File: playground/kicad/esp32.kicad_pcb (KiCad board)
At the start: 2 copper layers, 85 x 75 mm, 79 parts, among them J1 5 / 12V, J10 Red, J11 Green, J12 Blue, J13 White, J14 Pad, J15 CONN FT232RL, J16 RJ12-I2C, J17 RJ12-I2C, J18 BATT, J2 +12V, J3 Onewire, J4 Onewire, J5 hole, J6 hole, J7 hole, J8 hole, J9 IO_RGBW, Q1 BSP75, Q2 BSP75, Q3 BSP75, Q4 BSP75, SW1 RESET, SW2 PROG, U1 ESP32-WROOM-32U, U2 MS5637, U3 Si7020-A20, U4 MCP73831-2, U5 ACT4088, U6 ACT4088, U7 DS18B20U, U8 TCS3400

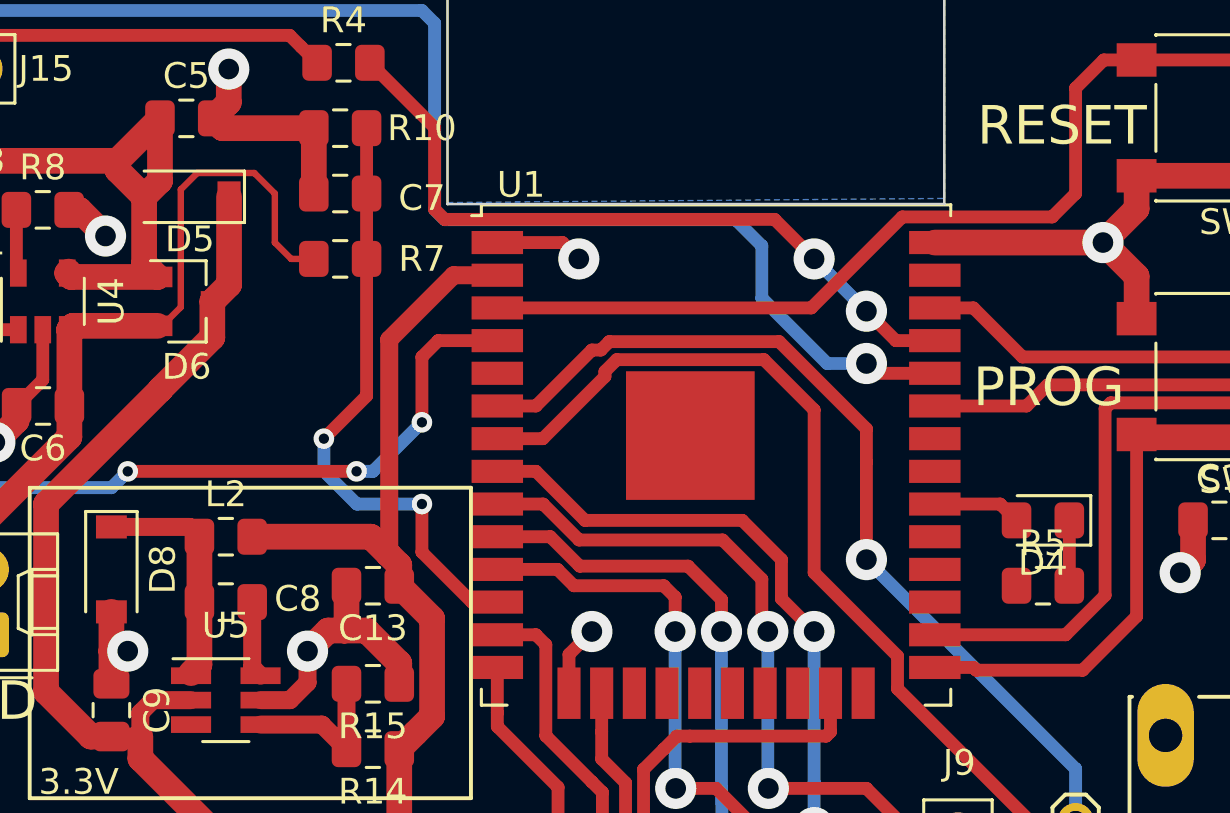
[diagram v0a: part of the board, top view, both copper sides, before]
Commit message: fix missing ground
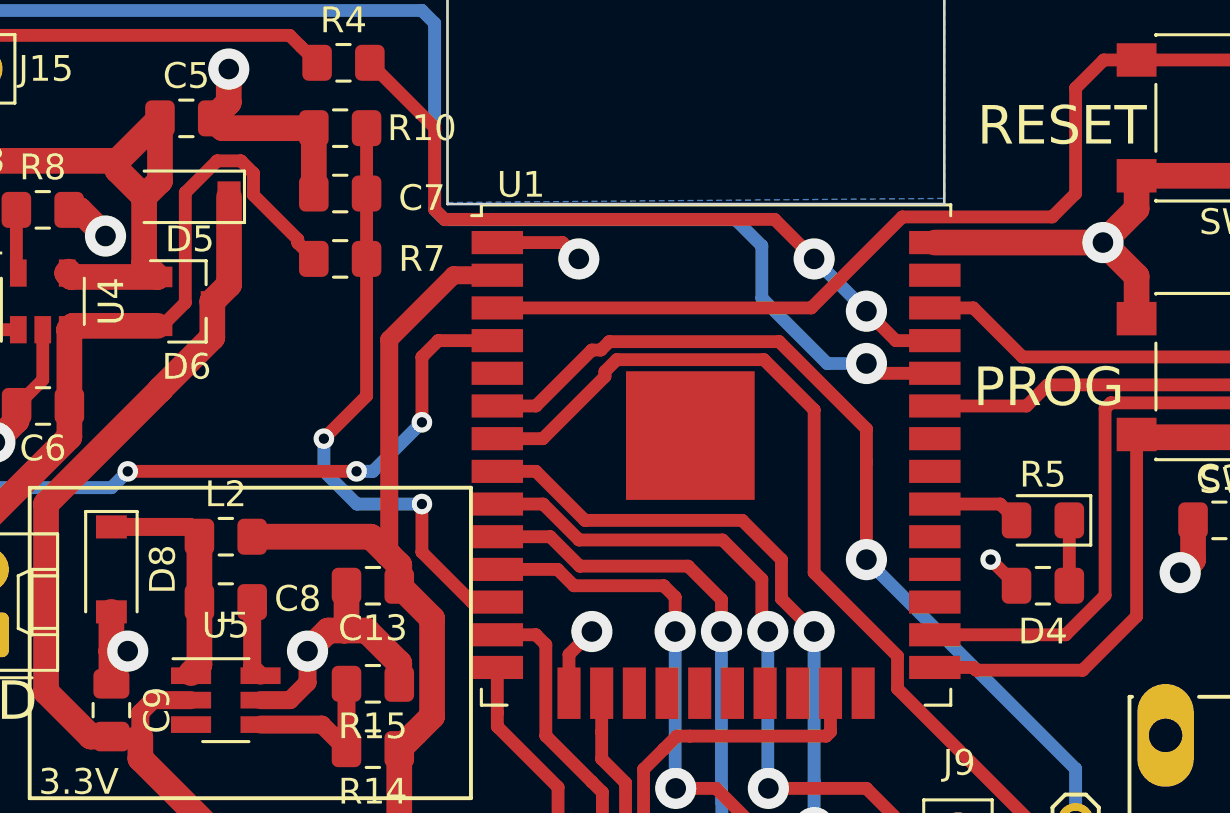
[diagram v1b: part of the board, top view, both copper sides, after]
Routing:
- net GND: track 113.9 -> 115.4 mm, vias 24 -> 25
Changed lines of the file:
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@@
     (thickness 1.6)
     (drawings 52)
-    (tracks 669)
+    (tracks 673)
     (zones 0)
     (modules 79)
@@
   )
   (setup
-    (last_trace_width 0.25)
+    (last_trace_width 0.5)
     (user_trace_width 0.25)
     (user_trace_width 0.5)
@@
     (tags "resistor handsolder")
     (attr smd)
-    (fp_text reference R5 (at 0 -1.65) (layer F.SilkS)
+    (fp_text reference R5 (at 0 -4.318) (layer F.SilkS)
       (effects (font (size 1 1) (thickness 0.15)))
     )
@@
     (tags "LED handsolder")
     (attr smd)
-    (fp_text reference D4 (at 0 -1.65 180) (layer F.SilkS)
+    (fp_text reference D4 (at 0 -4.318 180) (layer F.SilkS)
       (effects (font (size 1 1) (thickness 0.15)))
     )
@@
   (segment (start 158 120.881) (end 158.01 120.871) (width 0.25) (layer F.Cu) (net 1))
   (segment (start 158 122.075) (end 158 120.881) (width 0.25) (layer F.Cu) (net 1))
+  (segment (start 140.475 84.921) (end 139.468 83.914) (width 0.5) (layer F.Cu) (net 1))
+  (via (at 139.468 83.914) (size 0.8) (drill 0.4) (layers F.Cu B.Cu) (net 1))
+  (segment (start 140.475 84.93) (end 140.475 84.921) (width 0.5) (layer F.Cu) (net 1))
   (segment (start 103.738 72.931) (end 103.588 72.781) (width 1) (layer F.Cu) (net 2))
   (segment (start 107.1 72.931) (end 103.738 72.931) (width 1) (layer F.Cu) (net 2))
@@
   (segment (start 132.864 109.822) (end 138.198 109.822) (width 1.5) (layer F.Cu) (net 19))
   (segment (start 127.657 104.615) (end 132.864 109.822) (width 1.5) (layer F.Cu) (net 19))
-  (segment (start 107.276 74.831) (end 107.226 74.831) (width 0.25) (layer F.Cu) (net 19))
-  (segment (start 108.001001 74.105999) (end 107.276 74.831) (width 0.25) (layer F.Cu) (net 19))
-  (segment (start 108.001001 69.533999) (end 108.001001 74.105999) (width 0.25) (layer F.Cu) (net 19))
-  (segment (start 108.643001 68.891999) (end 108.001001 69.533999) (width 0.25) (layer F.Cu) (net 19))
-  (segment (start 110.856999 68.891999) (end 108.643001 68.891999) (width 0.25) (layer F.Cu) (net 19))
-  (segment (start 111.655 69.69) (end 110.856999 68.891999) (width 0.25) (layer F.Cu) (net 19))
-  (segment (start 111.655 71.595) (end 111.655 69.69) (width 0.25) (layer F.Cu) (net 19))
-  (segment (start 112.29 72.23) (end 111.655 71.595) (width 0.25) (layer F.Cu) (net 19))
-  (segment (start 113.17 72.23) (end 112.29 72.23) (width 0.25) (layer F.Cu) (net 19))
   (segment (start 100.225 82.59793) (end 100.225 84.295) (width 1) (layer F.Cu) (net 19))
   (segment (start 103.672 79.15093) (end 100.225 82.59793) (width 1) (layer F.Cu) (net 19))
@@
   (segment (start 97.05 91.28) (end 97.685 91.28) (width 1.5) (layer F.Cu) (net 19))
   (segment (start 95.984802 91.28) (end 97.05 91.28) (width 1.5) (layer F.Cu) (net 19))
+  (segment (start 112.546628 71.606628) (end 112.546628 71.470628) (width 0.5) (layer F.Cu) (net 19))
+  (segment (start 113.17 72.23) (end 112.546628 71.606628) (width 0.5) (layer F.Cu) (net 19))
+  (segment (start 110.82601 68.907008) (end 110.339002 68.42) (width 0.5) (layer F.Cu) (net 19))
+  (segment (start 110.82601 69.75001) (end 110.82601 68.907008) (width 0.5) (layer F.Cu) (net 19))
+  (segment (start 112.546628 71.470628) (end 110.82601 69.75001) (width 0.5) (layer F.Cu) (net 19))
+  (segment (start 107.276 74.831) (end 107.226 74.831) (width 0.5) (layer F.Cu) (net 19))
+  (segment (start 108.176 73.931) (end 107.276 74.831) (width 0.5) (layer F.Cu) (net 19))
+  (segment (start 108.176 69.656998) (end 108.176 73.931) (width 0.5) (layer F.Cu) (net 19))
+  (segment (start 109.412998 68.42) (end 108.176 69.656998) (width 0.5) (layer F.Cu) (net 19))
+  (segment (start 110.339002 68.42) (end 109.412998 68.42) (width 0.5) (layer F.Cu) (net 19))
   (segment (start 121.8 77.945) (end 123.974 75.771) (width 0.5) (layer F.Cu) (net 21))
   (segment (start 120.3 77.945) (end 121.8 77.945) (width 0.5) (layer F.Cu) (net 21))

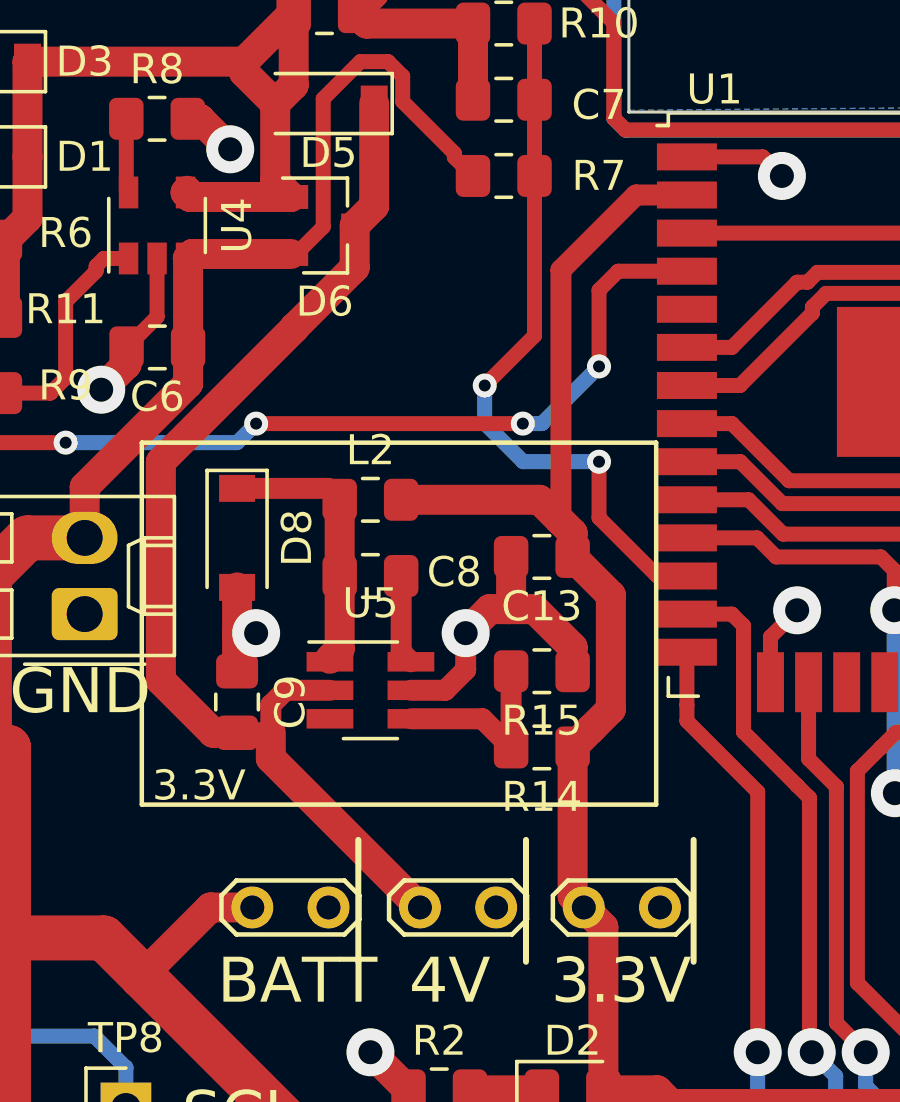
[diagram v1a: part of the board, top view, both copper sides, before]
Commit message: fix: close https://github.com/Hackuarium/esp-32wroom/issues/13
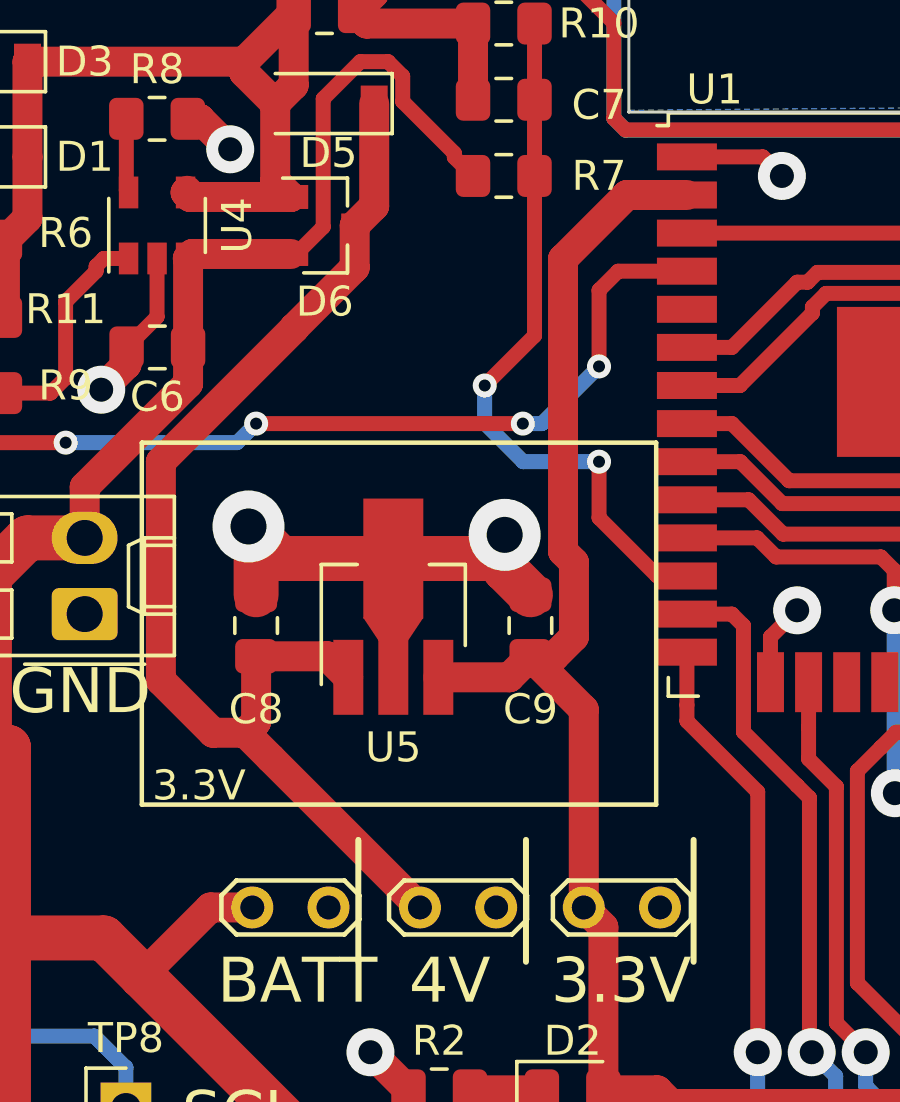
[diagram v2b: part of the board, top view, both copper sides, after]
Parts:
- removed C13: 22µF, Capacitor_SMD:C_0805_2012Metric_Pad1.15x1.40mm_HandSolder
- removed D8: B240A, Diode_SMD:D_SOD-123
- removed L2: 4.7µH, Inductor_SMD:L_0805_2012Metric_Pad1.15x1.40mm_HandSolder
- removed R14: 49.9k, Resistor_SMD:R_0805_2012Metric_Pad1.15x1.40mm_HandSolder
- removed R15: 16.23k, Resistor_SMD:R_0805_2012Metric_Pad1.15x1.40mm_HandSolder
- C8: value 22nF -> C
- C9: value 10µF -> C
- R4: value 499 -> 1k
- U5: value ACT4088 -> AP7365-33YG; footprint Package_TO_SOT_SMD:SOT-23-6_Handsoldering -> Package_TO_SOT_SMD:SOT-89-3_Handsoldering
- moved C9 10.1 mm to (115.1, 87.2)
- moved C8 4.15 mm to (105.9, 87.2), turned to 90 degrees
- moved U5 2.53 mm to (110.5, 87.0), turned to 90 degrees
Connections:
- net /ONE2 renamed ONE2
- C8 pad 1: Net-(C8-Pad1) -> /AP7365-33YG/VIN
- C8 pad 2: Net-(C8-Pad2) -> GND
- C9 pad 1: /ACT4088-33/VIN -> +3V3
- D5 pad 1: /ACT4088-33/VIN -> /AP7365-33YG/VIN
- D6 pad 3: /ACT4088-33/VIN -> /AP7365-33YG/VIN
- J3 pad T: /ONE1 -> ONE1
- R1 pad 2: /ONE1 -> ONE1
- R17 pad 2: ONE3 -> ONE1
- TP1 pad 1: /ONE1 -> ONE1
- TP3 pad 1: /ACT4088-33/VIN -> /AP7365-33YG/VIN
- U1 pad 26: ONE3 -> ONE1
- U1 pad 6: /ONE1 -> ONE1
- U5 pad 1: Net-(C8-Pad2) -> /AP7365-33YG/VIN
- U5 pad 2: /ACT4088-33/VIN -> GND
- U5 pad 3: Net-(U5-Pad3) -> +3V3
- U7 pad 1: ONE3 -> ONE1
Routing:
- net ONE1: track 0.00 -> 132.6 mm, vias 0 -> 1
- net ONE3: track 79.0 -> 0.00 mm
- net /ONE1: track 53.5 -> 0.00 mm, vias 1 -> 0
- net /AP7365-33YG/VIN: track 0.00 -> 40.0 mm
- net /ACT4088-33/VIN: track 37.5 -> 0.00 mm
- net Net-(C8-Pad2): track 9.01 -> 0.00 mm
- net Net-(R14-Pad2): track 6.28 -> 0.00 mm
- net Net-(C8-Pad1): track 2.99 -> 0.00 mm
- net +3V3: track 171.6 -> 170.1 mm

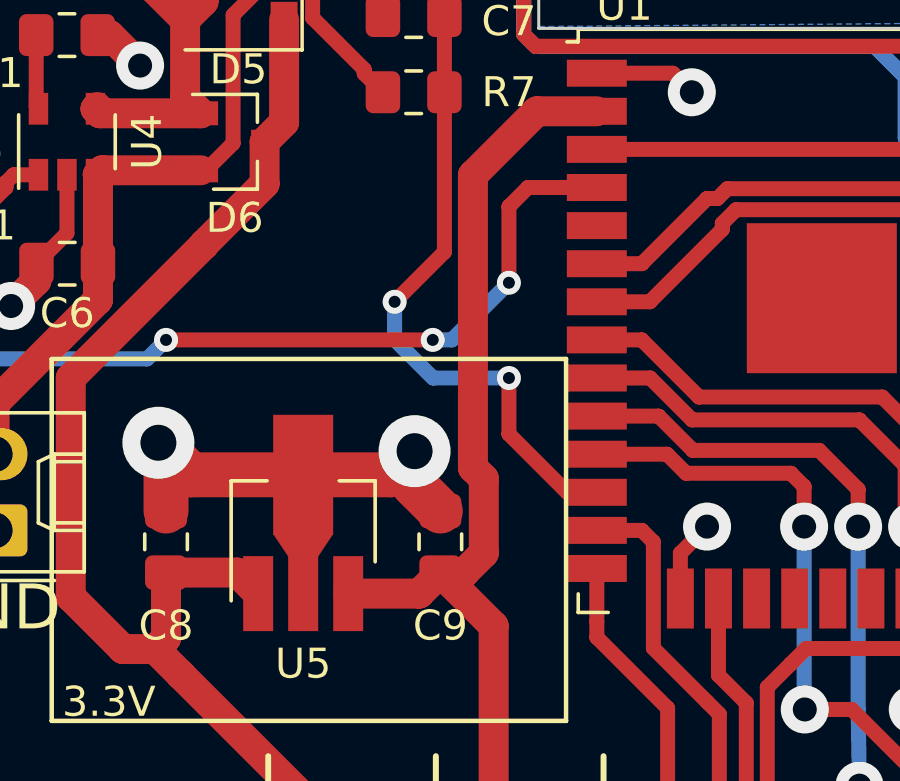
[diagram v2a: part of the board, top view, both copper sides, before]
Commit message: fix: close https://github.com/Hackuarium/esp-32wroom/issues/8
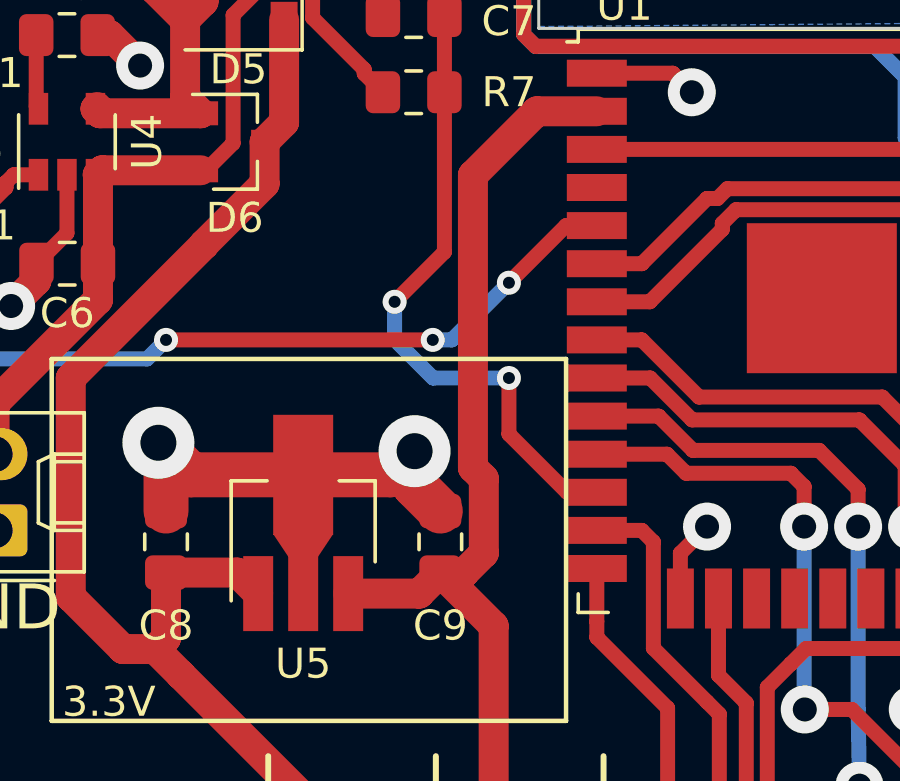
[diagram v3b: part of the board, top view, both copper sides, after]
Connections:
- U1 pad 4: CHARGING -> Net-(U1-Pad4)
- U1 pad 5: Net-(U1-Pad5) -> CHARGING
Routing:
- net GND: track 115.2 -> 119.2 mm
- net CHARGING: track 32.3 -> 30.3 mm

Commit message: fix: rename One1 to One3
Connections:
- R17 pad 2: ONE1 -> ONE3
- U1 pad 26: ONE1 -> ONE3
- U7 pad 1: ONE1 -> ONE3
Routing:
- net ONE3: track 0.00 -> 79.0 mm
- net ONE1: track 132.6 -> 53.5 mm
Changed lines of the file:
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@@
     (zones 0)
     (modules 74)
-    (nets 75)
+    (nets 76)
   )
   (page A4)
@@
   (net 73 /AP7365-33YG/VIN)
   (net 74 "Net-(U1-Pad4)")
+  (net 75 ONE3)
   (net_class Default "This is the default net class."
     (clearance 0.2)
@@
     (add_net ONE1)
     (add_net ONE2)
+    (add_net ONE3)
     (add_net SCL)
     (add_net SDA)
@@
       (net 66 "Net-(U7-Pad2)"))
     (pad 1 smd rect (at -2.2 -0.975 180) (size 1.45 0.45) (layers F.Cu F.Paste F.Mask)
-      (net 71 ONE1))
+      (net 75 ONE3))
     (model ${KISYS3DMOD}/Package_SO.3dshapes/MSOP-8_3x3mm_P0.65mm.wrl
       (at (xyz 0 0 0))
@@
     (fp_line (start -1 0.6) (end -1 -0.6) (layer F.Fab) (width 0.1))
     (pad 2 smd roundrect (at 1.025 0) (size 1.15 1.4) (layers F.Cu F.Paste F.Mask) (roundrect_rratio 0.217391)
-      (net 71 ONE1))
+      (net 75 ONE3))
     (pad 1 smd roundrect (at -1.025 0) (size 1.15 1.4) (layers F.Cu F.Paste F.Mask) (roundrect_rratio 0.217391)
       (net 3 +3V3))
@@
       (net 34 /IO0))
     (pad 26 smd rect (at 8.5 6.985) (size 2 0.9) (layers F.Cu F.Paste F.Mask)
-      (net 71 ONE1))
+      (net 75 ONE3))
     (pad 27 smd rect (at 8.5 5.715) (size 2 0.9) (layers F.Cu F.Paste F.Mask)
       (net 26 "Net-(U1-Pad27)"))
@@
   (segment (start 151.336 94.074) (end 153.565 91.845) (width 0.5) (layer F.Cu) (net 71))
   (segment (start 142.77 94.074) (end 151.336 94.074) (width 0.5) (layer F.Cu) (net 71))
-  (segment (start 143.914999 78.041999) (end 144.132988 77.82401) (width 0.5) (layer F.Cu) (net 71))
-  (segment (start 143.914999 85.304967) (end 143.914999 78.041999) (width 0.5) (layer F.Cu) (net 71))
-  (segment (start 142.384966 86.835) (end 143.914999 85.304967) (width 0.5) (layer F.Cu) (net 71))
-  (segment (start 137.3 86.835) (end 142.384966 86.835) (width 0.5) (layer F.Cu) (net 71))
-  (segment (start 144.132988 77.82401) (end 157.502 77.82401) (width 0.5) (layer F.Cu) (net 71))
-  (segment (start 157.76201 77.82401) (end 159.21499 79.27699) (width 0.5) (layer F.Cu) (net 71))
-  (segment (start 157.502 77.82401) (end 157.76201 77.82401) (width 0.5) (layer F.Cu) (net 71))
-  (segment (start 159.153 119.474) (end 159.21499 119.53599) (width 0.5) (layer F.Cu) (net 71))
-  (segment (start 157.003 119.474) (end 159.153 119.474) (width 0.5) (layer F.Cu) (net 71))
-  (segment (start 159.21499 79.27699) (end 159.21499 119.53599) (width 0.5) (layer F.Cu) (net 71))
-  (segment (start 159.089002 124.046) (end 158.899 124.046) (width 0.5) (layer F.Cu) (net 71))
-  (segment (start 159.21499 123.920012) (end 159.089002 124.046) (width 0.5) (layer F.Cu) (net 71))
-  (segment (start 159.21499 119.53599) (end 159.21499 123.920012) (width 0.5) (layer F.Cu) (net 71))
-  (segment (start 159.085001 124.050001) (end 158 124.050001) (width 0.5) (layer F.Cu) (net 71))
-  (segment (start 159.21499 123.920012) (end 159.085001 124.050001) (width 0.5) (layer F.Cu) (net 71))
+  (segment (start 143.914999 78.041999) (end 144.132988 77.82401) (width 0.5) (layer F.Cu) (net 75))
+  (segment (start 143.914999 85.304967) (end 143.914999 78.041999) (width 0.5) (layer F.Cu) (net 75))
+  (segment (start 142.384966 86.835) (end 143.914999 85.304967) (width 0.5) (layer F.Cu) (net 75))
+  (segment (start 137.3 86.835) (end 142.384966 86.835) (width 0.5) (layer F.Cu) (net 75))
+  (segment (start 144.132988 77.82401) (end 157.502 77.82401) (width 0.5) (layer F.Cu) (net 75))
+  (segment (start 157.76201 77.82401) (end 159.21499 79.27699) (width 0.5) (layer F.Cu) (net 75))
+  (segment (start 157.502 77.82401) (end 157.76201 77.82401) (width 0.5) (layer F.Cu) (net 75))
+  (segment (start 159.153 119.474) (end 159.21499 119.53599) (width 0.5) (layer F.Cu) (net 75))
+  (segment (start 157.003 119.474) (end 159.153 119.474) (width 0.5) (layer F.Cu) (net 75))
+  (segment (start 159.21499 79.27699) (end 159.21499 119.53599) (width 0.5) (layer F.Cu) (net 75))
+  (segment (start 159.089002 124.046) (end 158.899 124.046) (width 0.5) (layer F.Cu) (net 75))
+  (segment (start 159.21499 123.920012) (end 159.089002 124.046) (width 0.5) (layer F.Cu) (net 75))
+  (segment (start 159.21499 119.53599) (end 159.21499 123.920012) (width 0.5) (layer F.Cu) (net 75))
+  (segment (start 159.085001 124.050001) (end 158 124.050001) (width 0.5) (layer F.Cu) (net 75))
+  (segment (start 159.21499 123.920012) (end 159.085001 124.050001) (width 0.5) (layer F.Cu) (net 75))
   (segment (start 153.565 104.52) (end 153.565 106.12) (width 0.5) (layer F.Cu) (net 72))
   (segment (start 143.54201 109.07001) (end 148.11499 109.07001) (width 0.5) (layer F.Cu) (net 72))

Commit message: chore: update labels
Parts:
- moved R2 11.6 mm to (108.2, 91.8)
- moved D2 11.6 mm to (112.7, 91.8)
- moved C8 0.76 mm to (105.9, 86.5)
- moved C9 0.76 mm to (115.1, 86.5)
- moved U5 0.76 mm to (110.5, 86.2)
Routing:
- net GND: track 119.2 -> 123.2 mm, vias 25 -> 24
- net +3V3: track 170.1 -> 174.1 mm
- net /AP7365-33YG/VIN: track 40.0 -> 43.5 mm
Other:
- board text added: "ESP-32 Playground 1.2"
- board text added: "OW1"
- board text added: "OW2"
- board text added: "VIN"
- board text added: "VIN 5-24V"
- board text removed: "12V"
- board text removed: "ESP-32 Playground 1.1"
- board text removed: "OW"
